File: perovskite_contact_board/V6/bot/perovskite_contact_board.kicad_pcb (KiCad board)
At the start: 2 copper layers, 53.2 x 53.2 mm, 10 parts, among them U1 Perovskite_CP_6_Cell, U2 Perovskite_CP_6_Cell, U3 Perovskite_CP_6_Cell, U7 BME280

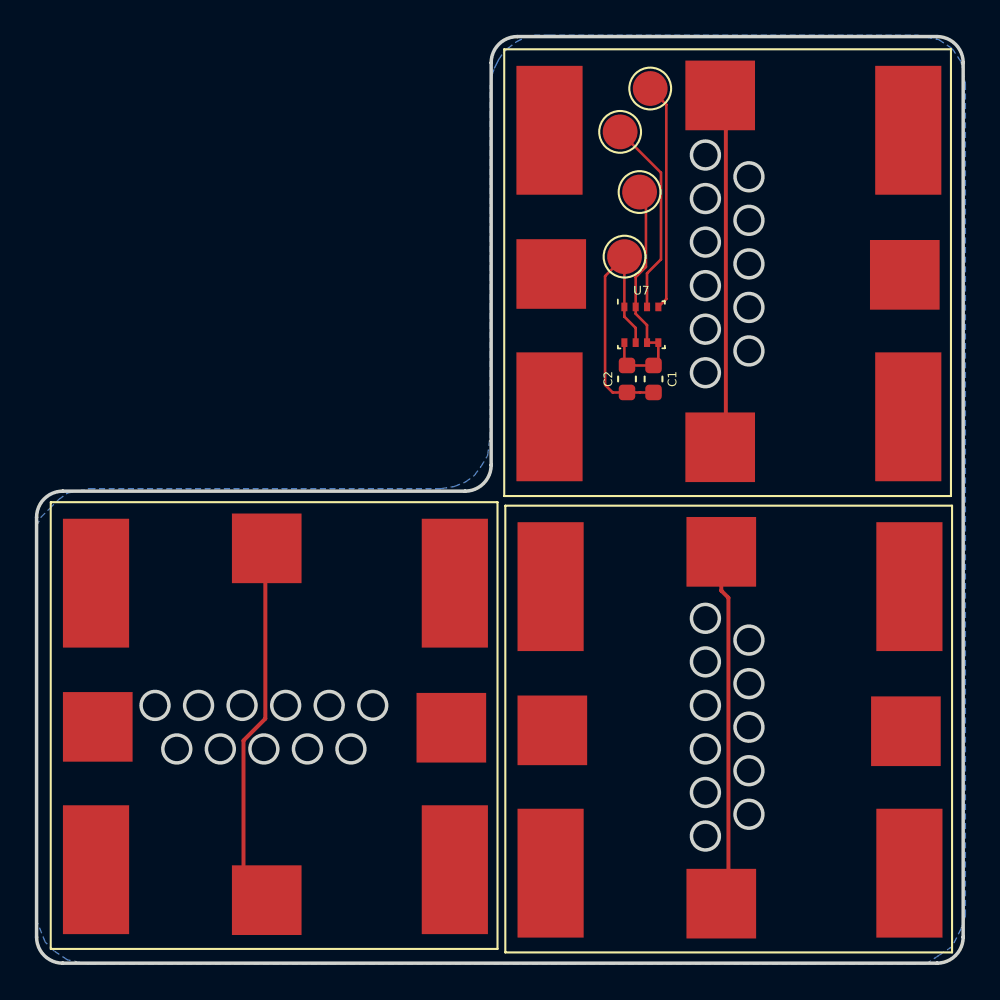
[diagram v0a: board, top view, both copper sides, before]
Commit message: Updated pogo pin contact boards
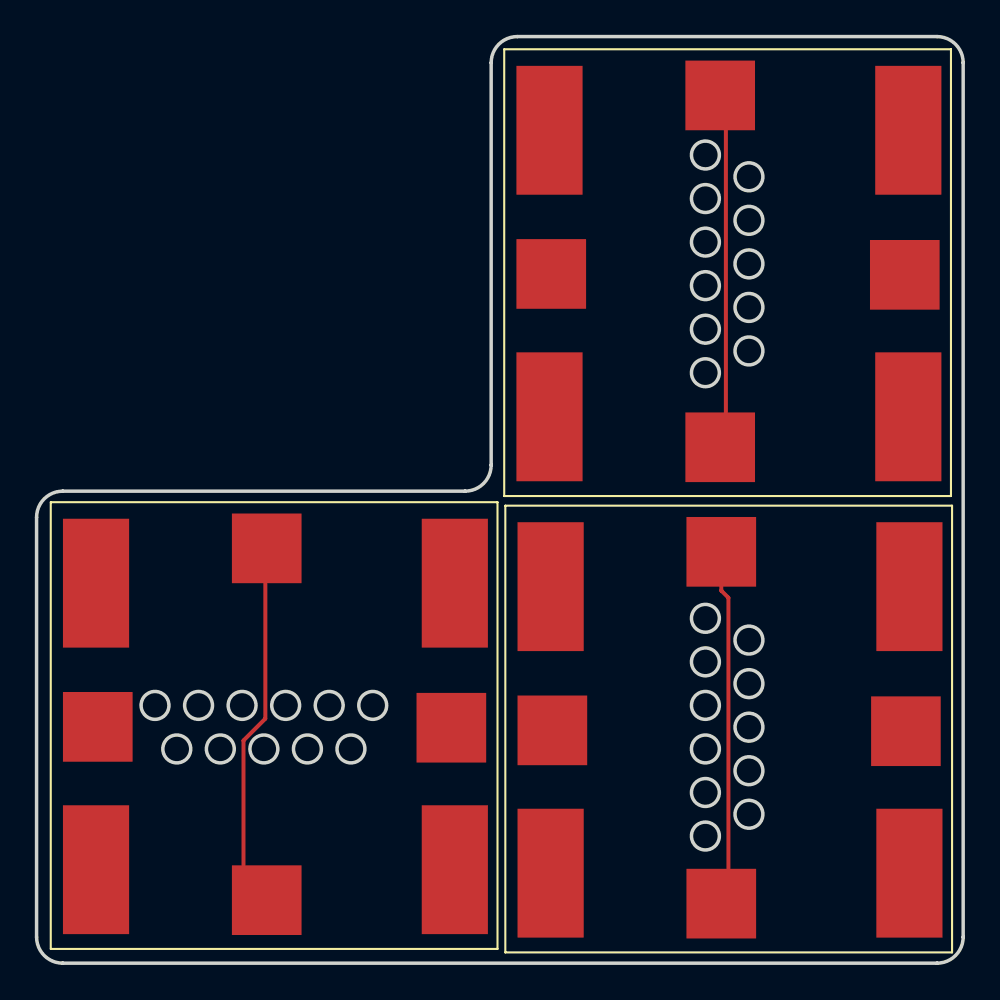
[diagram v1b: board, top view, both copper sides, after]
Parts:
- removed C1, C2: 0.1u, Capacitor_SMD:C_0603_1608Metric
- removed JP103.1, JP103.11, JP103.2, JP103.8: Conn_01x01, TestPoint:TestPoint_Pad_D2.0mm
- removed U7: BME280, Package_LGA:Bosch_LGA-8_2.5x2.5mm_P0.65mm_ClockwisePinNumbering
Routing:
- net GND: track 16.0 -> 0.00 mm
- net VDD: track 14.3 -> 0.00 mm
- net SCL3: track 13.1 -> 0.00 mm
- net SDA2: track 11.4 -> 0.00 mm
- removed copper zone on B.Cu, net GND
